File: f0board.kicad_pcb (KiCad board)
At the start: 2 copper layers, 31 x 18.3 mm, 28 parts, among them P1 CONN_12, P2 CONN_12, SW1 SW_PUSH, U1 STM32F303CCT6, U2 MCP1700, U3 MAX3051, X1 XTAL-SMD-4-PADS

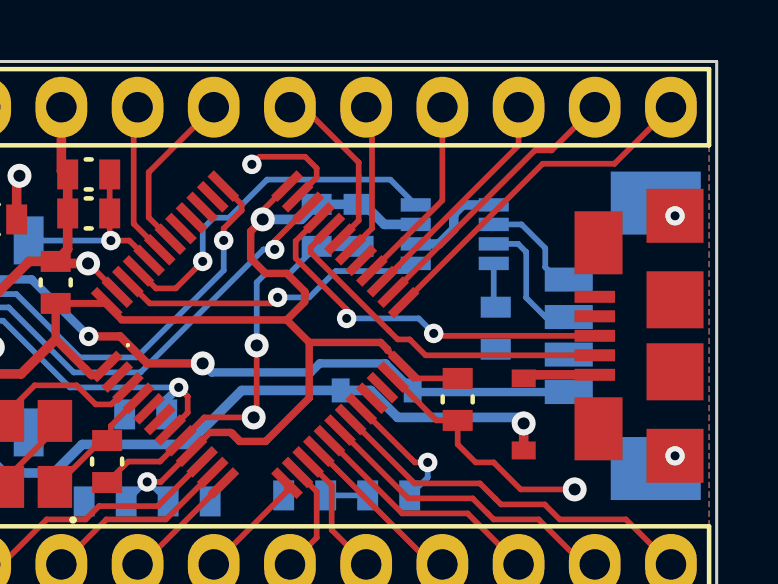
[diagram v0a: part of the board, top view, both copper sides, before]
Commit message: Additional GND via.
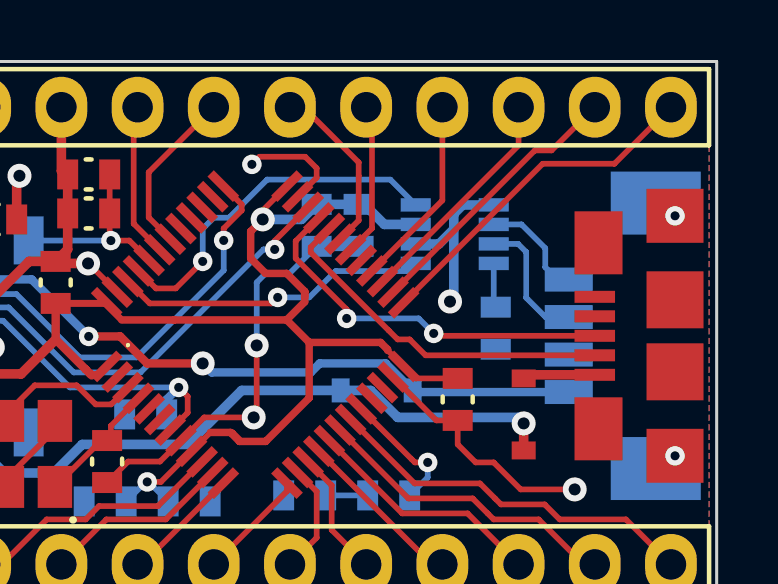
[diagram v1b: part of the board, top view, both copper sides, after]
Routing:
- net GND: track 61.2 -> 63.6 mm, vias 10 -> 11

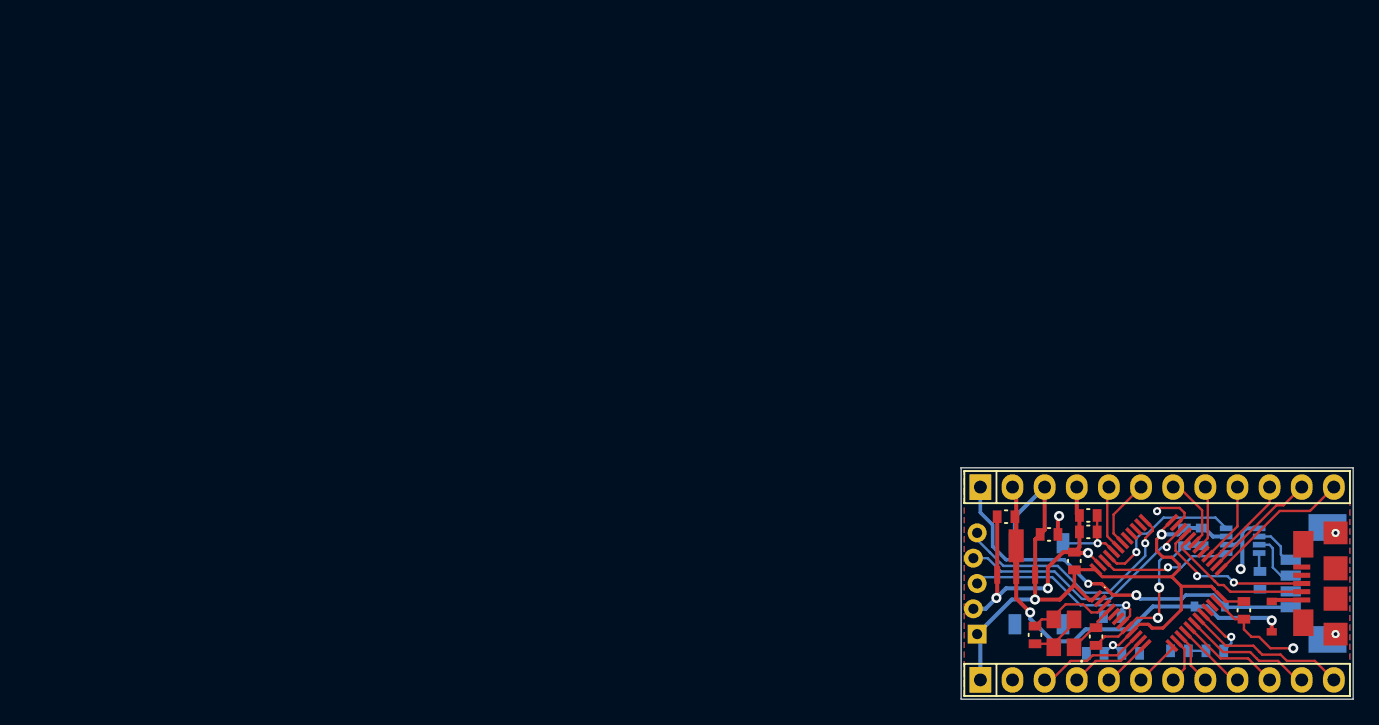
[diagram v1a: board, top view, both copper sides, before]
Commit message: Place board near to origin.
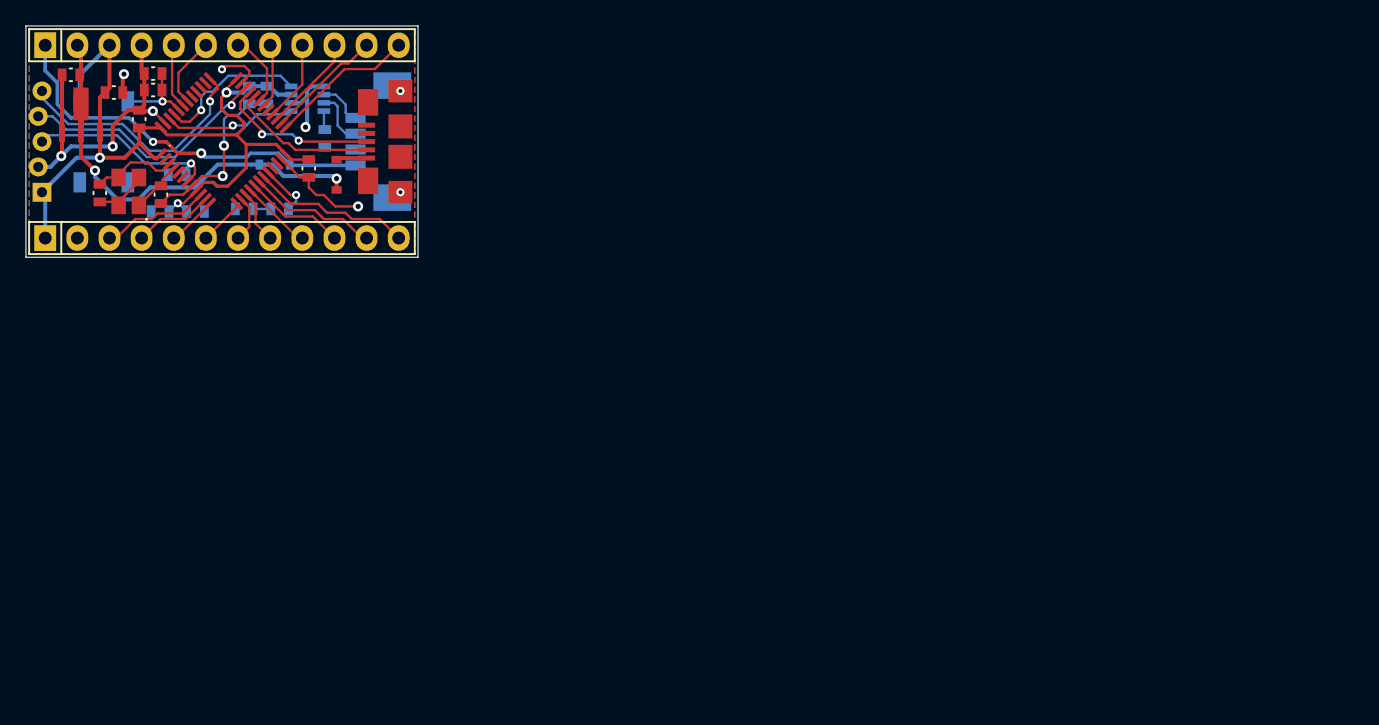
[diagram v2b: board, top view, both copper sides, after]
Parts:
- moved C1 81.7 mm to (37.5, 29.6)
- moved CONN3 81.7 mm to (54.4, 33.7)
- moved D1 81.7 mm to (47.5, 39.0)
- moved D2 81.7 mm to (52.0, 36.3)
- moved R2 81.7 mm to (37.5, 28.3)
- moved C10 81.7 mm to (33.3, 37.7)
- moved C11 81.7 mm to (31.0, 28.4)
- moved C2 81.7 mm to (46.5, 30.0)
- moved C5 81.7 mm to (49.8, 35.8)
- moved C6 81.7 mm to (40.8, 39.2)
- moved C8 81.7 mm to (38.0, 39.2)
- moved CONN1 81.7 mm to (28.7, 33.7)
- moved D3 81.7 mm to (47.1, 35.5)
- moved P1 81.7 mm to (42.9, 26.0)
- moved P2 81.7 mm to (42.9, 41.3)
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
